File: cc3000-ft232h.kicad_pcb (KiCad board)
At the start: 2 copper layers, 50 x 50 mm, 7 parts, among them P1 CONN_4X2, U1 U.FL_U.FL, U2 CC3000TEXAS_CC3000

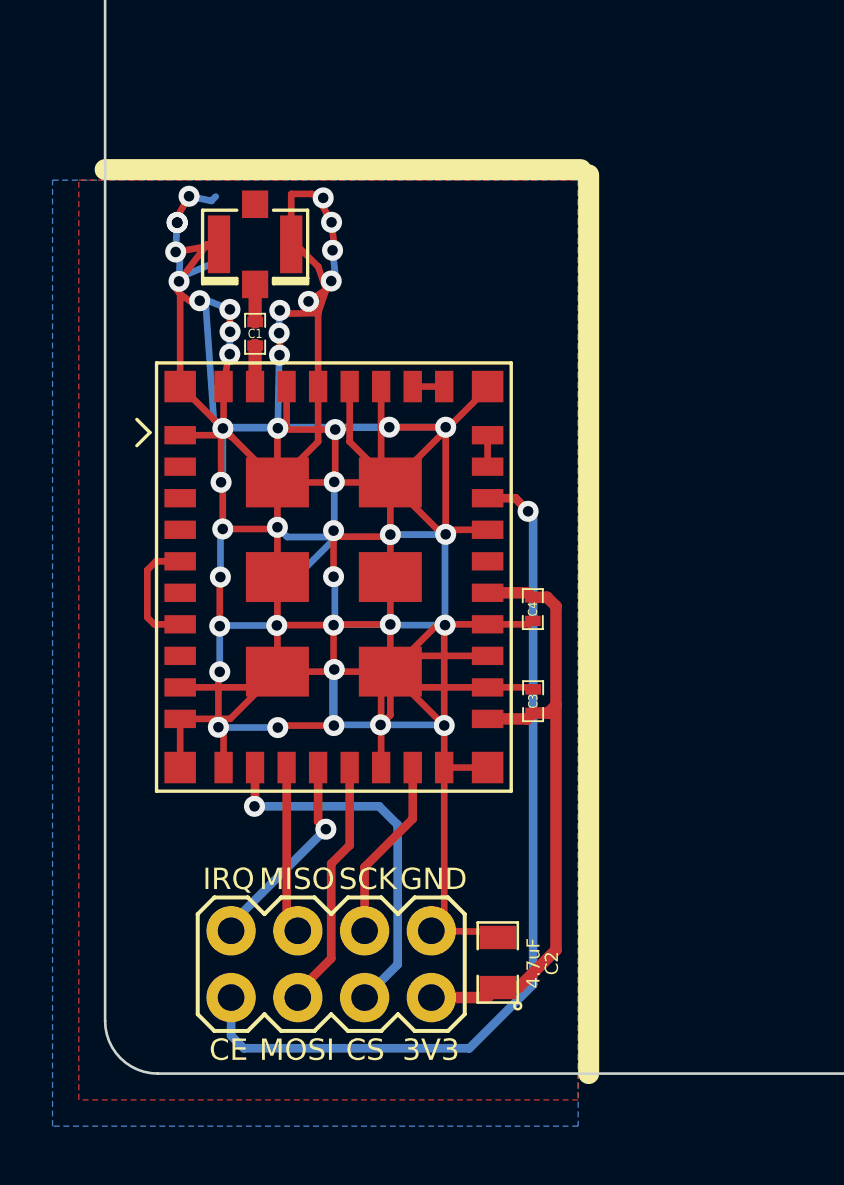
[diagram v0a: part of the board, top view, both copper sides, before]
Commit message: pinheader for breadboard
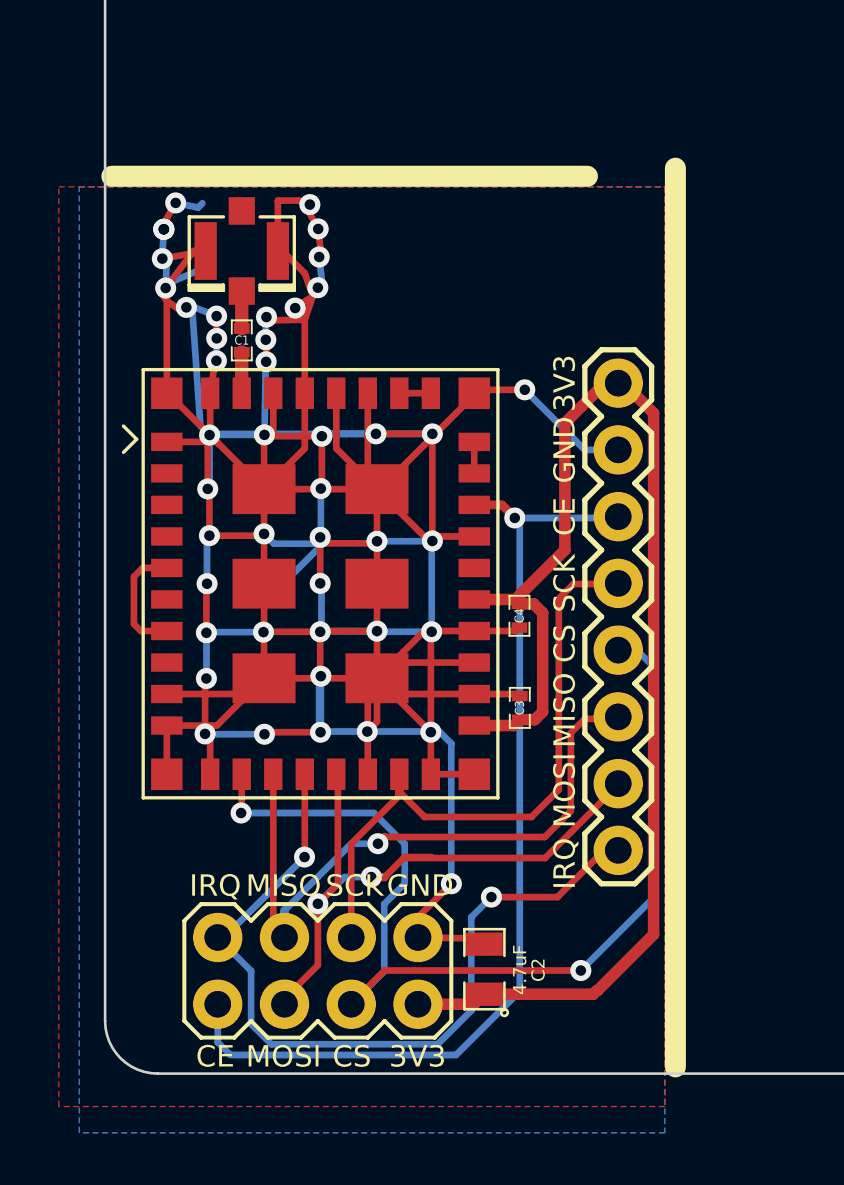
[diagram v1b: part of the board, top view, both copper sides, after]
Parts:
- added P2: CONN_8, 1X08, F.Cu at (144.5, 93.7)
- moved C4 0.57 mm to (140.8, 102.6)
- moved P1 0.57 mm to (133.1, 116.1)
- moved U2 0.57 mm to (133.2, 101.4)
- moved C1 0.57 mm to (130.2, 92.1)
- moved C2 0.57 mm to (139.4, 116.0)
- moved U1 0.57 mm to (130.2, 88.7)
- moved C3 0.57 mm to (140.8, 106.1)
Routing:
- net +3.3V: track 24.2 -> 51.4 mm
- net /cc3000/SPI_CS: track 14.3 -> 38.7 mm, vias 1 -> 2
- net /cc3000/SPI_IRQ: track 7.83 -> 31.0 mm, vias 1 -> 2
- net /cc3000/SPI_MISO: track 6.39 -> 24.9 mm, vias 0 -> 1
- net /cc3000/SPI_CLK: track 6.97 -> 24.3 mm
- net /cc3000/SPI_MOSI: track 9.57 -> 24.0 mm, vias 0 -> 2
- net GND: track 238.1 -> 247.2 mm, vias 43 -> 45
- net /cc3000/VBAT_SW_EN: track 34.0 -> 38.0 mm

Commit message: added ft232h sheet
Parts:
- added C5: 0.1, SM0805, F.Cu at (182.6, 113.8)
- added CON1: USB-MINI-B, USB-MINIB, F.Cu at (175.1, 120.1)
- added P3: CONN_11, 1X11_LOCK, F.Cu at (148.8, 90.8)
- added P4: CONN_11, 1X11_LOCK, F.Cu at (173.4, 116.2)
- added U3: FT232H, QFN48, F.Cu at (160.8, 97.4)
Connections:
- U2 pad 2: N-000006 -> (no net)
- U2 pad 24: N-000005 -> (no net)
- U2 pad 3: N-0000019 -> (no net)
- U2 pad 4: N-0000011 -> (no net)
- U2 pad 6: N-000002 -> (no net)
- U2 pad 8: N-000003 -> (no net)

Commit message: files_added
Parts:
- removed CON1: USB-MINI-B, USB-MINIB
- added U4: USB-MINIB-5PIN_USB-MINIB, USB-MINIB, F.Cu at (175.1, 120.1)
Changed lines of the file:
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@@
 (kicad_pcb (version 3) (host pcbnew "(2013-04-19 BZR 4011)-stable")
   (general
-    (links 89)
-    (no_connects 35)
+    (links 94)
+    (no_connects 40)
     (area 124.949999 69.949999 175.050001 120.050001)
     (thickness 1.6)
@@
   (net 31 N-000001)
   (net 32 N-0000010)
-  (net 33 N-0000048)
-  (net 34 N-0000053)
-  (net 35 N-0000055)
-  (net 36 N-0000056)
-  (net 37 N-0000059)
-  (net 38 N-0000060)
+  (net 33 N-0000053)
+  (net 34 N-0000055)
+  (net 35 N-0000057)
+  (net 36 N-0000059)
+  (net 37 N-0000060)
+  (net 38 N-0000062)
   (net 39 N-0000066)
   (net 40 N-0000068)
@@
     (add_net N-000001)
     (add_net N-0000010)
-    (add_net N-0000048)
     (add_net N-0000053)
     (add_net N-0000055)
-    (add_net N-0000056)
+    (add_net N-0000057)
     (add_net N-0000059)
     (add_net N-0000060)
+    (add_net N-0000062)
     (add_net N-0000066)
     (add_net N-0000068)
@@
     (pad 1 smd rect (at -3.39852 -2.74828 315) (size 0.59944 0.24892)
       (layers F.Cu F.Paste F.Mask)
-      (net 35 N-0000055)
+      (net 34 N-0000055)
     )
     (pad 2 smd rect (at -3.39852 -2.2479 315) (size 0.59944 0.24892)
       (layers F.Cu F.Paste F.Mask)
-      (net 33 N-0000048)
+      (net 38 N-0000062)
     )
     (pad 3 smd rect (at -3.39852 -1.74752 315) (size 0.59944 0.24892)
@@
     (pad 5 smd rect (at -3.39852 -0.7493 315) (size 0.59944 0.24892)
       (layers F.Cu F.Paste F.Mask)
-      (net 34 N-0000053)
+      (net 33 N-0000053)
     )
     (pad 6 smd rect (at -3.39852 -0.24892 315) (size 0.59944 0.24892)
@@
     (pad 12 smd rect (at -3.39852 2.75082 315) (size 0.59944 0.24892)
       (layers F.Cu F.Paste F.Mask)
-      (net 38 N-0000060)
+      (net 37 N-0000060)
     )
     (pad 33 smd rect (at 3.39852 -1.25222 315) (size 0.59944 0.24892)
@@
     (pad 34 smd rect (at 3.39852 -1.75006 315) (size 0.59944 0.24892)
       (layers F.Cu F.Paste F.Mask)
-      (net 37 N-0000059)
+      (net 36 N-0000059)
     )
     (pad 35 smd rect (at 3.39852 -2.25044 315) (size 0.59944 0.24892)
@@
     (pad 24 smd rect (at 2.75082 3.40106 315) (size 0.24892 0.59944)
       (layers F.Cu F.Paste F.Mask)
-      (net 38 N-0000060)
+      (net 37 N-0000060)
     )
     (pad 13 smd rect (at -2.74828 3.40106 315) (size 0.24892 0.59944)
@@
     (pad 37 smd rect (at 2.75082 -3.39852 315) (size 0.24892 0.59944)
       (layers F.Cu F.Paste F.Mask)
-      (net 36 N-0000056)
+      (net 35 N-0000057)
     )
     (pad 38 smd rect (at 2.25044 -3.39852 315) (size 0.24892 0.59944)
@@
     (pad 46 smd rect (at -1.75006 -3.39852 315) (size 0.24892 0.59944)
       (layers F.Cu F.Paste F.Mask)
-      (net 38 N-0000060)
+      (net 37 N-0000060)
     )
     (pad 47 smd rect (at -2.2479 -3.39852 315) (size 0.24892 0.59944)
@@
     (at 175.050001 120.055001)
     (descr "<b>USB Series Mini-B Surface Mounted</b>")
-    (fp_text reference CON1 (at -2.9972 -1.0668) (layer Eco1.User)
+    (fp_text reference U4 (at -2.9972 -1.0668) (layer Eco1.User)
       (effects (font (size 0.4064 0.4064) (thickness 0.03048)))
     )
-    (fp_text value USB-MINI-B (at -2.5908 0.2032) (layer Eco1.User)
+    (fp_text value USB-MINIB-5PIN_USB-MINIB (at -2.5908 0.2032) (layer Eco1.User)
       (effects (font (size 0.4064 0.4064) (thickness 0.03048)))
     )
@@
     (pad GND smd rect (at 2.49936 1.59766) (size 2.49936 0.49784)
       (layers F.Cu F.Paste F.Mask)
+      (net 30 GND)
     )
     (pad ID smd rect (at 2.49936 0.79756) (size 2.49936 0.49784)
@@
     (pad MTN3 smd rect (at -2.99974 4.49834) (size 2.49936 1.99898)
       (layers F.Cu F.Paste F.Mask)
+      (net 30 GND)
     )
     (pad MTN1 smd rect (at -2.99974 -4.49834) (size 2.49936 1.99898)
       (layers F.Cu F.Paste F.Mask)
+      (net 30 GND)
     )
     (pad MTN4 smd rect (at 2.49936 4.49834) (size 2.49936 1.99898)
       (layers F.Cu F.Paste F.Mask)
+      (net 30 GND)
     )
     (pad MTN2 smd rect (at 2.49936 -4.49834) (size 2.49936 1.99898)
       (layers F.Cu F.Paste F.Mask)
+      (net 30 GND)
     )
     (pad VBUS smd rect (at 2.49936 -1.59766) (size 2.49936 0.49784)

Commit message: files_added
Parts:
- added C10: 0.1, SM0805, F.Cu at (157.3, 90.2)
- added C11: 0.1, SM0805, B.Cu at (166.0, 101.2)
- added C12: 0.01, SM0805, F.Cu at (157.3, 92.0)
- added C13: 0.1, SM0805, F.Cu at (157.3, 86.6)
- added C14: 0.01, SM0805, F.Cu at (157.3, 88.4)
- added C6: 27p, SM0402, F.Cu at (198.6, 124.4)
- added C7: 27p, SM0402, F.Cu at (193.8, 119.8)
- added C8: 0.1, SM0805, F.Cu at (182.4, 122.8)
- added C9: 0.1, SM0805, F.Cu at (179.3, 118.1)
- added P5: CONN_4, 1X04_LOCK, F.Cu at (192.2, 112.4)
- added P6: CONN_4, 1X04_LOCK, F.Cu at (192.4, 103.6)
- added P7: CONN_6, 1X04_LOCK, F.Cu at (175.1, 120.1)
- added P8: CONN_4, 1X04_LOCK, F.Cu at (192.2, 107.6)
- added R1: 12K, SM0805, B.Cu at (166.0, 98.0)
- added R2: 12K, SM0805, F.Cu at (194.2, 125.8)
- added R3: 2K2, SM0805, B.Cu at (163.3, 97.5)
- added U5: 93LC56CX-X/SN_SOIC8-N_MC, SSOP8, B.Cu at (160.8, 100.6)
- moved U4 36.8 mm to (200.0, 93.0)
- moved P4 1.40 mm to (172.0, 116.3)
- moved P3 0.40 mm to (149.2, 90.8)
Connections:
- U3 pad 43: (no net) -> /ft232h/EEDATA
- U3 pad 44: (no net) -> /ft232h/EE_CK
- U3 pad 45: (no net) -> /ft232h/EE_CS
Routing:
- net /ft232h/EEDATA: track 0.00 -> 6.01 mm, vias 0 -> 1
- net /ft232h/EE_CS: track 0.00 -> 5.65 mm, vias 0 -> 1
- net /ft232h/EE_CK: track 0.00 -> 4.91 mm, vias 0 -> 1
- net GND: track 247.2 -> 252.1 mm
- net +3.3V: track 51.4 -> 54.7 mm
- net /ft232h/EE_DO: track 0.00 -> 1.55 mm

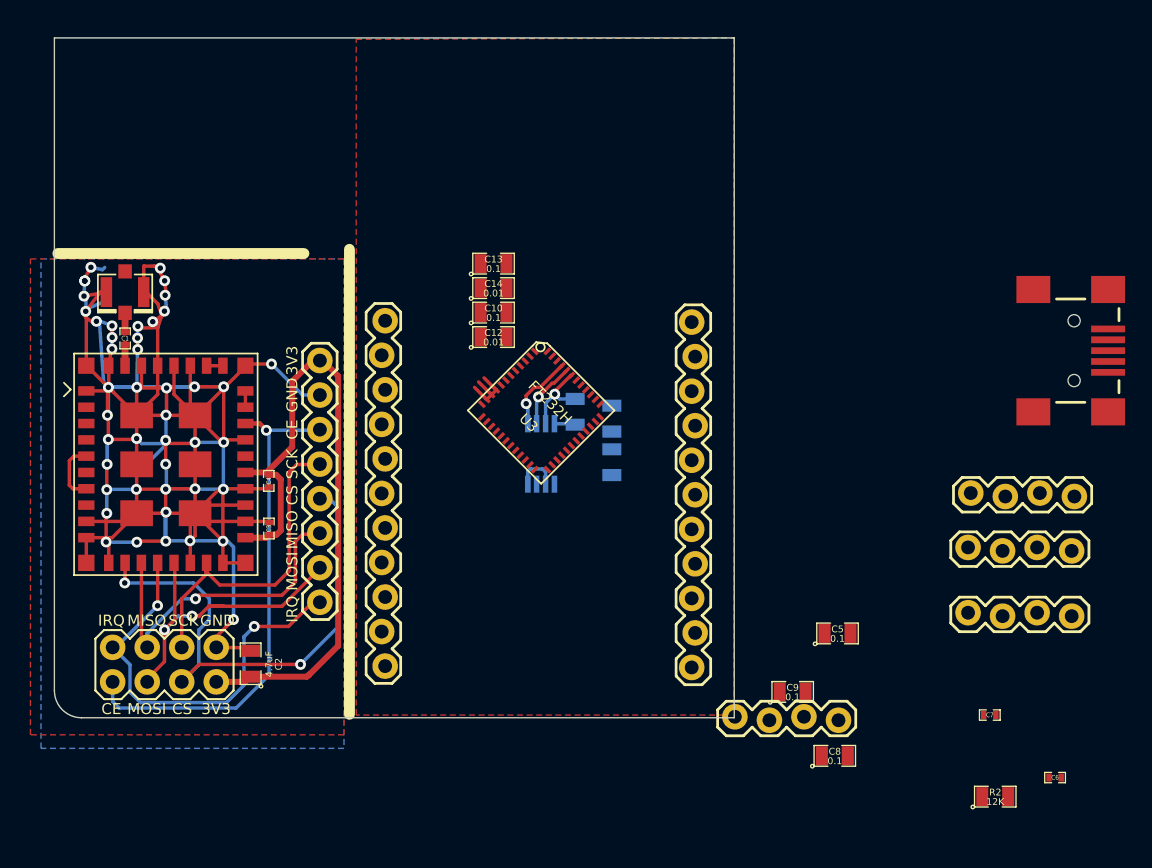
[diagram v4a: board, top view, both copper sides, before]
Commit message: crystal lib added , fixed mini-usb
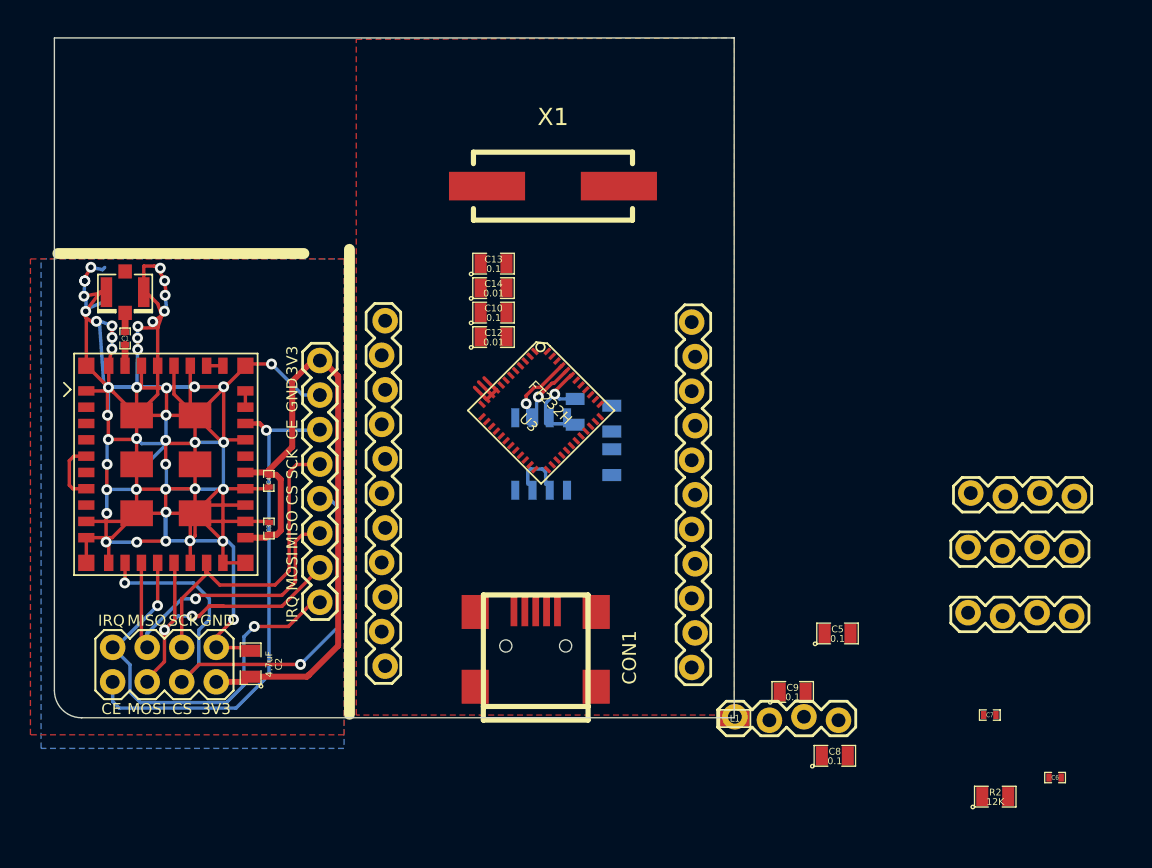
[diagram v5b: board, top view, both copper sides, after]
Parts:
- removed U4: USB-MINIB-5PIN_USB-MINIB, USB-MINIB
- added CON1: USB-MINI-B, USB_MINI_B, F.Cu at (160.4, 115.6)
- added L1: INDUCTOR_SMALL, SM0603, F.Cu at (175.1, 120.1)
- added X1: 12MHz, Crystal_HC49-SD_SMD_RevA_09Aug2010, F.Cu at (161.7, 80.9)
- U5: footprint SSOP8 -> SO8E
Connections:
- P3 pad 1: (no net) -> N-0000022
- P3 pad 11: (no net) -> N-0000019
- P4 pad 1: (no net) -> N-0000020
- P4 pad 11: (no net) -> N-0000034
- P7 pad 3: (no net) -> /ft232h/TDI
- P7 pad 4: (no net) -> /ft232h/TDO
- U2 pad 2: (no net) -> N-000006
- U2 pad 24: (no net) -> N-000005
- U2 pad 3: (no net) -> N-0000018
- U2 pad 4: (no net) -> N-0000011
- U2 pad 6: (no net) -> N-000002
- U2 pad 8: (no net) -> N-000003
- U3 pad 6: (no net) -> /ft232h/USB_D-
- U3 pad 7: (no net) -> /ft232h/USB_D+
- U5 pad 7: (no net) -> N-0000055
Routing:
- net (no net): track 0.00 -> 3.31 mm
- net +3.3V: track 54.7 -> 51.4 mm

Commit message: updated
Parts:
- removed L1: INDUCTOR_SMALL, SM0603
- added C15: 4.7u, SM0805, F.Cu at (175.1, 120.1)
- added C16: 0.1, SM0805, F.Cu at (175.1, 120.1)
- added FB1, FB2, FB3: FILTER, SM0805, F.Cu at (175.1, 120.1)
- added R4, R5, R6: 10K, SM0805, F.Cu at (175.1, 120.1)
- C12, C14: value 0.01 -> 4.7u
- C5: value 0.1 -> 0.01
- moved CON1 41.6 mm to (161.4, 74.0), turned to 270 degrees
- moved C13 23.4 mm to (180.7, 85.8)
- moved C12 23.0 mm to (180.3, 93.1)
- moved C14 22.8 mm to (180.1, 87.9)
- moved C10 22.5 mm to (179.8, 90.2)
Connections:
- net N-0000068 renamed /ft232h/VCORE
- C10 pad 1: N-0000067 -> N-0000062
- C12 pad 1: N-0000067 -> N-0000062
- C13 pad 1: N-0000067 -> N-0000063
- C14 pad 1: N-0000067 -> N-0000063
- C5 pad 1: /ft232h/VDEVICE -> /ft232h/VBUS
- CON1 pad 4: N-0000052 -> (no net)
- P3 pad 1: N-0000022 -> (no net)
- P3 pad 11: N-0000019 -> (no net)
- P4 pad 1: N-0000020 (its old number) -> (no net)
- P4 pad 11: N-0000034 (its old number) -> (no net)
- P7 pad 3: /ft232h/TDI -> (no net)
- P7 pad 4: /ft232h/TDO -> (no net)
- R1 pad 1: N-0000067 -> /ft232h/VCC3V3
- U2 pad 2: N-000006 -> (no net)
- U2 pad 24: N-000005 -> (no net)
- U2 pad 3: N-0000018 -> (no net)
- U2 pad 4: N-0000011 (its old number) -> (no net)
- U2 pad 6: N-000002 -> (no net)
- U2 pad 8: N-000003 -> (no net)
- U3 pad 12: N-0000064 -> /ft232h/VCC3V3
- U3 pad 24: N-0000064 -> /ft232h/VCC3V3
- U3 pad 3: N-0000067 -> N-0000063
- U3 pad 39: N-0000067 -> /ft232h/VCC3V3
- U3 pad 46: N-0000064 -> /ft232h/VCC3V3
- U3 pad 8: N-0000067 -> N-0000062
- U5 pad 6: +3.3V -> /ft232h/VCC3V3
- U5 pad 7: N-0000055 -> (no net)
- U5 pad 8: +3.3V -> /ft232h/VCC3V3

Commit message: headers
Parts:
- removed P6, P8: CONN_4, 1X04_LOCK
- added D1: LED, LED-0603, F.Cu at (161.7, 103.5)
- added D2: LED, LED-0603, F.Cu at (164.5, 103.5)
- added IC1: V_REG_LM1117SOT223, SparkFun-SOT223, B.Cu at (152.2, 79.0)
- added JP1: JUMPER, 1X02_LOCK, F.Cu at (153.9, 109.4)
- added JP2: JUMPER, 1X02_LOCK, F.Cu at (164.2, 109.3)
- added JP3: JUMPER, 1X02_LOCK, F.Cu at (153.9, 106.8)
- added JP4: JUMPER, 1X02_LOCK, F.Cu at (153.8, 104.3)
- added R10: 10K, SM0603, B.Cu at (159.1, 105.1)
- added R11: R, SM0603, F.Cu at (164.5, 104.9)
- added R12: R, SM0603, F.Cu at (161.7, 104.9)
- added R7: 12K, SM0603, B.Cu at (151.1, 71.6)
- added R8: 12K, SM0603, B.Cu at (151.1, 73.5)
- added R9: 10K, SM0603, B.Cu at (159.1, 106.8)
- P3, P4: value CONN_11 -> CONN_13; footprint 1X11_LOCK -> 1X13
- P7: footprint 1X04_LOCK -> 1X06_LOCK
- moved C6 53.3 mm to (162.3, 85.4), turned to 180 degrees
- moved C7 49.5 mm to (158.2, 85.4)
- moved P5 38.3 mm to (154.0, 114.5)
- moved FB1 35.6 mm to (170.8, 84.7), turned to 180 degrees
- moved FB3 34.4 mm to (154.8, 92.3), turned to 90 degrees
- moved R1 27.7 mm to (177.7, 72.9)
- moved C12 22.7 mm to (157.7, 90.9)
- moved U5 22.1 mm to (167.5, 79.5), turned to 270 degrees
- moved C10 22.1 mm to (157.7, 89.3)
- moved P7 21.2 mm to (154.1, 116.9)
- moved C13 20.0 mm to (161.0, 89.3)
- moved C14 19.3 mm to (161.0, 90.9)
- moved R3 18.9 mm to (172.6, 81.0)
- moved C11 17.3 mm to (182.9, 97.7)
- moved R4 15.4 mm to (190.4, 120.9)
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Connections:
- net /ft232h/V_OUT renamed N-0000058
- C5 pad 1: /ft232h/VBUS -> +5V
- CON1 pad 1: /ft232h/VBUS -> +5V
- FB1 pad 1: /ft232h/VBUS -> +5V
- P3 pad 1: (no net) -> +5V
- P3 pad 10: /ft232h/ACBUS0 -> /ft232h/ADBUS7
- P3 pad 11: (no net) -> /ft232h/ACBUS0
- P3 pad 2: /ft232h/ADBUS0 -> GND
- P3 pad 3: /ft232h/ADBUS1 -> /ft232h/ADBUS0
- P3 pad 4: /ft232h/ADBUS2 -> /ft232h/ADBUS1
- P3 pad 5: /ft232h/ADBUS3 -> /ft232h/ADBUS2
- P3 pad 6: /ft232h/ADBUS4 -> /ft232h/ADBUS3
- P3 pad 7: /ft232h/ADBUS5 -> /ft232h/ADBUS4
- P3 pad 8: /ft232h/ADBUS6 -> /ft232h/ADBUS5
- P3 pad 9: /ft232h/ADBUS7 -> /ft232h/ADBUS6
- P4 pad 1: (no net) -> +3.3V
- P4 pad 10: /ft232h/ACBUS9 -> /ft232h/ACBUS8
- P4 pad 11: (no net) -> /ft232h/ACBUS9
- P4 pad 2: /ft232h/ACBUS1 -> GND
- P4 pad 3: /ft232h/ACBUS2 -> /ft232h/ACBUS1
- P4 pad 4: /ft232h/ACBUS3 -> /ft232h/ACBUS2
- P4 pad 5: /ft232h/ACBUS4 -> /ft232h/ACBUS3
- P4 pad 6: /ft232h/ACBUS5 -> /ft232h/ACBUS4
- P4 pad 7: /ft232h/ACBUS6 -> /ft232h/ACBUS5
- P4 pad 8: /ft232h/ACBUS7 -> /ft232h/ACBUS6
- P4 pad 9: /ft232h/ACBUS8 -> /ft232h/ACBUS7
- P5 pad 3: /ft232h/SDA -> /ft232h/ADBUS1
- P5 pad 4: /ft232h/SCL -> /ft232h/ADBUS0
- P7 pad 3: (no net) -> /ft232h/ADBUS1
- P7 pad 4: (no net) -> /ft232h/ADBUS0
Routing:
- net GND: track 252.1 -> 316.9 mm, vias 45 -> 46
- net +5V: track 0.00 -> 51.4 mm, vias 0 -> 1
- net +3.3V: track 51.4 -> 100.3 mm, vias 0 -> 2
- net /ft232h/ACBUS1: track 0.00 -> 19.7 mm
- net /ft232h/ACBUS0: track 0.00 -> 18.5 mm
- net /ft232h/ADBUS7: track 0.00 -> 17.2 mm
- net /ft232h/ACBUS2: track 0.00 -> 16.4 mm
- net /ft232h/EE_CS: track 5.65 -> 20.8 mm
- net /ft232h/EE_CK: track 4.91 -> 19.3 mm
- net /ft232h/EEDATA: track 6.01 -> 20.3 mm
- net /ft232h/VREGIN: track 0.00 -> 13.6 mm
- net N-0000054: track 0.00 -> 13.3 mm
- net N-0000049: track 0.00 -> 13.0 mm
- net /ft232h/ACBUS9: track 0.00 -> 11.9 mm
- net /ft232h/ACBUS8: track 0.00 -> 11.2 mm
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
